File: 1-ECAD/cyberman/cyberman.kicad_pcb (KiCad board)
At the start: 4 copper layers, 39.7 x 69.6 mm, 123 parts, among them J1001 532610271, J801 5033981892, J901 YXT-BB10-24S-02, SW801 SKRMAAE010, SW802 SKRMAAE010, SW803 SKRMAAE010, SW804 SKRMAAE010, SW805 SKRMAAE010, SW806 SKRMAAE010, U1001 MAX98357A, U1002 ICS-43434, U1003 LIS2MDLTR, U1004 LSM6DSOTR, U16 1054500101, U18 PM254-2-10-W-8.5, U401 ESP32-S3R16V, U501 ESP32-S3R16V, U503 W25Q128JWPIQ, U504 1054500101, U601 BQ27220YZFR, U602 BQ25896RTWR, U604 RS3221-3.3YF3, U607 LM3281YFQR, U608 LM3281YFQR, U609 MMDT2907A-7-F, U801 PM254-2-10-W-8.5

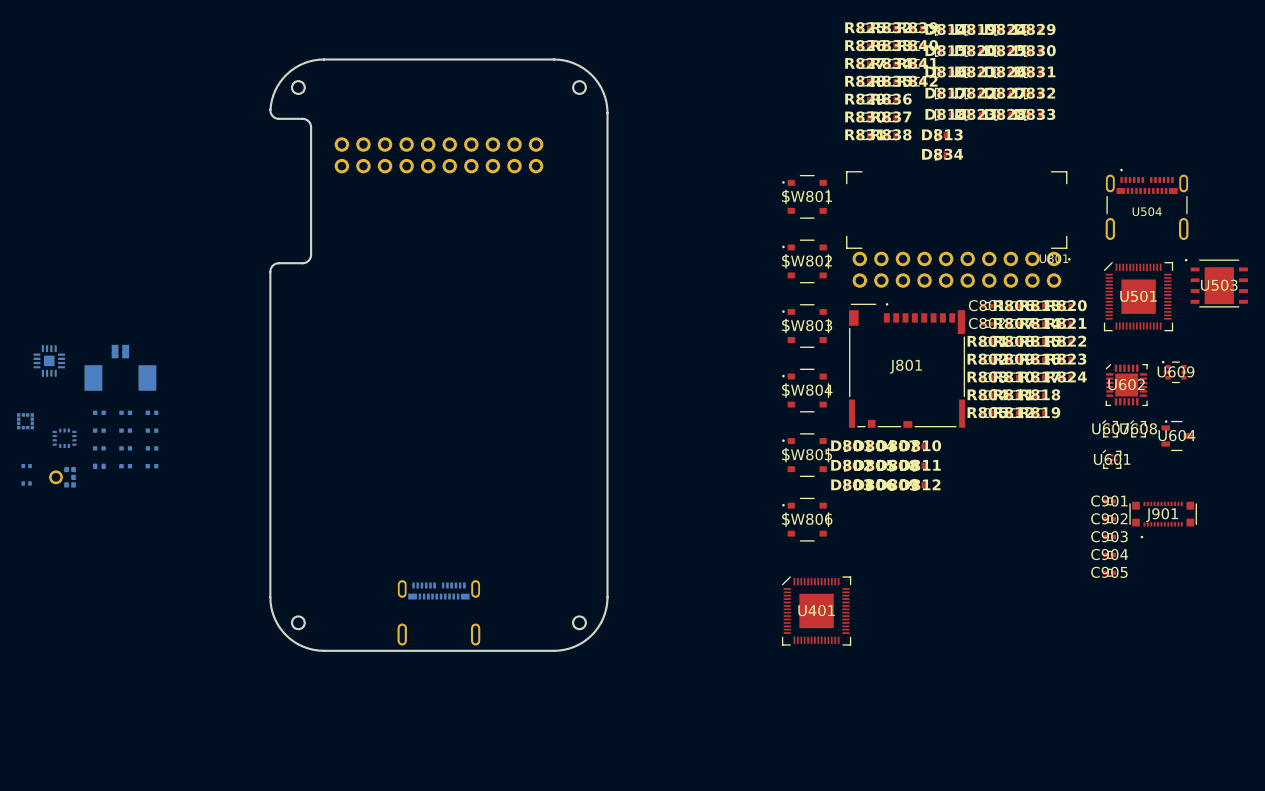
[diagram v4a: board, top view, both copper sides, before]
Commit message: add fuse and place external connector
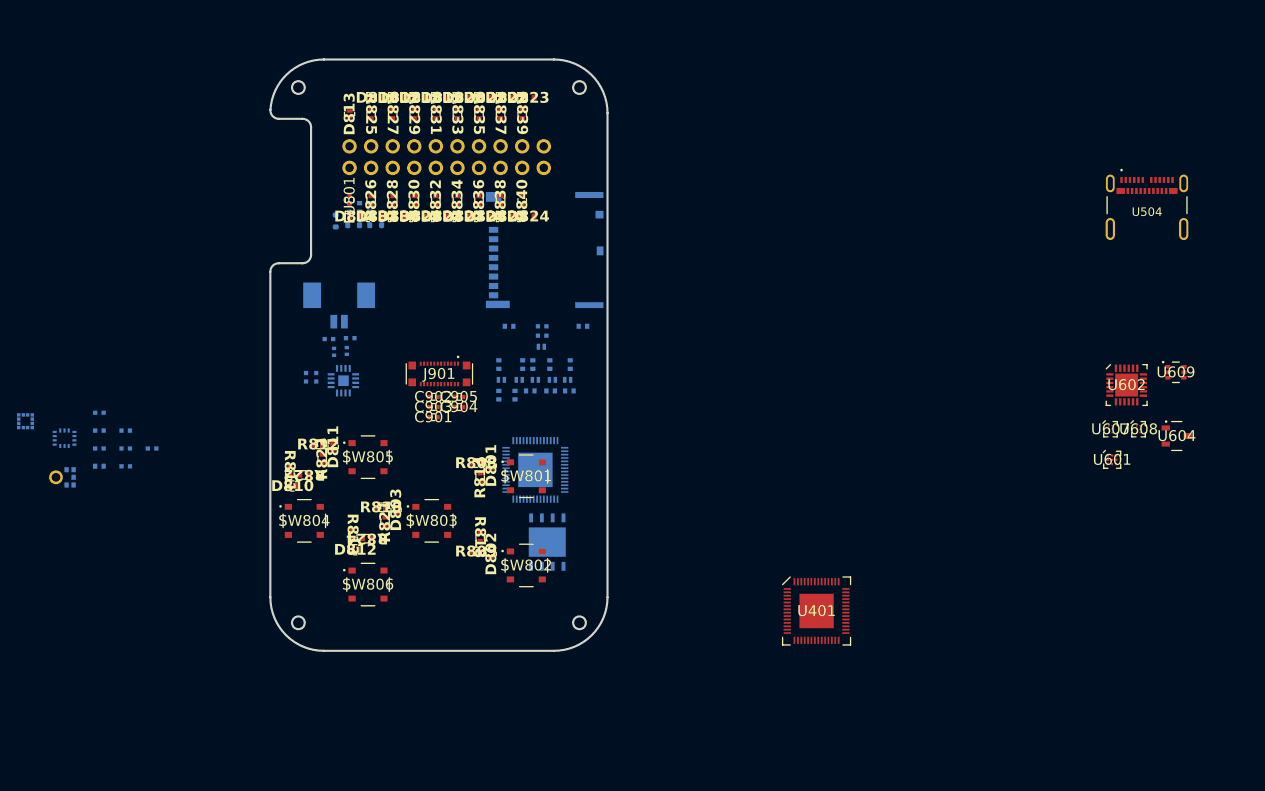
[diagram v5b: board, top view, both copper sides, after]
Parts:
- removed D834: LESD8D3.3CAT5G, 0_diode_smd:LESD8D3.3CAT5G
- removed U16: 1054500101, 0_connector_smd:1054500101
- removed U18: PM254-2-10-W-8.5, 0_connector_smd:PM254-2-10-W-8.5
- added FU801: ERBRD2R00X, 0_fuses_smd:ERBRD0R63X, F.Cu at (128.3, 51.3)
- added FU802: ERBRD2R00X, 0_fuses_smd:ERBRD0R63X, B.Cu at (128.3, 52.1)
- C801, C802, D804, D805, D806, D807, D808, D809, D815, D832, D833, J801, R801, R802, R803, R804, R805, R806, R807, R815, R816, R817, R819, R820, R841, R842, U501, U503, U801: moved to B.Cu
- moved R822 91.1 mm to (123.0, 83.6), turned to 180 degrees
- moved R823 88.4 mm to (125.1, 81.7), turned to 90 degrees
- moved J901 86.8 mm to (138.9, 71.7)
- moved R811 85.7 mm to (121.3, 83.1), turned to -90 degrees
- moved R813 85.3 mm to (128.7, 90.6), turned to -90 degrees
- moved U503 84.7 mm to (151.6, 91.5), turned to 90 degrees
- moved R824 84.5 mm to (130.4, 91.1), turned to 180 degrees
- moved U801 84.0 mm to (128.3, 44.9), turned to 180 degrees
- moved R821 83.5 mm to (132.5, 89.1), turned to 90 degrees
- moved R812 82.0 mm to (124.6, 80.0)
- moved D832 81.7 mm to (128.8, 54.2), turned to 180 degrees
- moved C903 81.1 mm to (138.2, 75.6)
- moved C902 80.9 mm to (138.2, 74.4)
- moved C901 80.2 mm to (138.2, 76.8)
- moved C905 79.4 mm to (141.2, 74.4)
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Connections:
- D816 pad 1: /Project Architecture/Peripherals/U0TXD -> /Project Architecture/Peripherals/1
- D817 pad 1: /Project Architecture/Peripherals/U0RXD -> /Project Architecture/Peripherals/2
- D818 pad 1: /Project Architecture/Peripherals/U0TXD -> /Project Architecture/Peripherals/3
- D819 pad 1: /Project Architecture/Peripherals/U0RXD -> /Project Architecture/Peripherals/4
- D820 pad 1: /Project Architecture/Peripherals/U0TXD -> /Project Architecture/Peripherals/5
- D821 pad 1: /Project Architecture/Peripherals/U0RXD -> /Project Architecture/Peripherals/6
- D822 pad 1: /Project Architecture/Peripherals/U0TXD -> /Project Architecture/Peripherals/7
- D823 pad 1: /Project Architecture/Peripherals/U0RXD -> /Project Architecture/Peripherals/8
- D824 pad 1: /Project Architecture/Peripherals/U0RXD -> /Project Architecture/Peripherals/16
- D825 pad 1: /Project Architecture/Peripherals/U0TXD -> /Project Architecture/Peripherals/15
- D826 pad 1: /Project Architecture/Peripherals/U0RXD -> /Project Architecture/Peripherals/14
- D827 pad 1: /Project Architecture/Peripherals/U0TXD -> /Project Architecture/Peripherals/13
- D828 pad 1: /Project Architecture/Peripherals/U0RXD -> /Project Architecture/Peripherals/12
- D829 pad 1: /Project Architecture/Peripherals/U0TXD -> /Project Architecture/Peripherals/11
- D830 pad 1: /Project Architecture/Peripherals/U0RXD -> /Project Architecture/Peripherals/10
- D831 pad 1: /Project Architecture/Peripherals/U0TXD -> /Project Architecture/Peripherals/9
- R825 pad 1: /Project Architecture/Peripherals/U0TXD -> /Project Architecture/Peripherals/1
- R826 pad 1: /Project Architecture/Peripherals/U0TXD -> /Project Architecture/Peripherals/9
- R827 pad 1: /Project Architecture/Peripherals/U0RXD -> /Project Architecture/Peripherals/2
- R828 pad 1: /Project Architecture/Peripherals/U0RXD -> /Project Architecture/Peripherals/10
- R829 pad 1: /Project Architecture/Peripherals/U0TXD -> /Project Architecture/Peripherals/3
- R830 pad 1: /Project Architecture/Peripherals/U0TXD -> /Project Architecture/Peripherals/11
- R831 pad 1: /Project Architecture/Peripherals/U0RXD -> /Project Architecture/Peripherals/4
- R832 pad 1: /Project Architecture/Peripherals/U0RXD -> /Project Architecture/Peripherals/12
- R833 pad 1: /Project Architecture/Peripherals/U0TXD -> /Project Architecture/Peripherals/5
- R834 pad 1: /Project Architecture/Peripherals/U0TXD -> /Project Architecture/Peripherals/13
- R835 pad 1: /Project Architecture/Peripherals/U0RXD -> /Project Architecture/Peripherals/6
- R836 pad 1: /Project Architecture/Peripherals/U0RXD -> /Project Architecture/Peripherals/14
- R837 pad 1: /Project Architecture/Peripherals/U0TXD -> /Project Architecture/Peripherals/7
- R838 pad 1: /Project Architecture/Peripherals/U0TXD -> /Project Architecture/Peripherals/15
- R839 pad 1: /Project Architecture/Peripherals/U0RXD -> /Project Architecture/Peripherals/8
- R840 pad 1: /Project Architecture/Peripherals/U0RXD -> /Project Architecture/Peripherals/16

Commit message: change layout
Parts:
- removed U401: ESP32-S3R16V, 0_mcu_espressif:ESP32-S3R16V
- U504, U601, U602, U604, U607, U608, U609: moved to B.Cu
- moved U504 96.1 mm to (138.8, 100.4), turned to 180 degrees
- moved U604 67.2 mm to (163.6, 104.6), turned to 180 degrees
- moved U609 67.0 mm to (163.7, 97.1), turned to 180 degrees
- moved U608 58.9 mm to (168.1, 103.8), turned to 180 degrees
- moved U602 56.4 mm to (169.5, 98.6), turned to 180 degrees
- moved U601 53.4 mm to (171.2, 107.4), turned to 180 degrees
- moved U607 53.1 mm to (171.4, 103.8), turned to 180 degrees
- moved U1003 48.9 mm to (138.4, 69.4), turned to 0 degrees
- moved U1004 46.0 mm to (138.4, 64.8), turned to 0 degrees
- moved C1010 43.6 mm to (139.5, 62.5)
- moved C1011 41.6 mm to (138.4, 67.4), turned to 0 degrees
- moved C1006 40.5 mm to (141.4, 69.2), turned to 90 degrees
- moved C1007 40.0 mm to (140.4, 69.2), turned to 90 degrees
- moved C1008 39.4 mm to (139.8, 71.4), turned to 0 degrees
- moved C1009 38.7 mm to (135.9, 65.0), turned to 90 degrees
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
